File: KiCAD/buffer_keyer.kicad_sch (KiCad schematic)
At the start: 56 parts, among them J1 Conn_01x02_Pin, J2 Conn_01x02_Pin, J3 Conn_01x02_Pin, T1 2N3906, T2 2N3906, U3 MC1496, U4 MCP4921, U6 LM7171xIN, U7 LM7171xIN, U8 MCP4728

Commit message: kicad(bias): build complete grid-bias sheet (Design A: dual OPA454)
New sheet untitled.kicad_sch (sheet name "Bias", file to be renamed
bias.kicad_sch) implementing the OPA454 high-voltage design per the
Grid_Bias_Schematic.pdf design doc:

- LM7805 (U9) generates the +5 V supply rail from +12 V (~30 mA load,
  no heatsink needed at ~270 mW dissipation)
- LM4040DIZ-5.0 (U11) generates a SEPARATE +5 V_REF precision reference
  biased from +12 V via R_Z = 2.2 kΩ; cathode bypassed by C23 (100 nF).
  Drives only R_GA / R_GB (the two OPA454 summing-junction inputs) and
  the cathode-monitor's 1.5 V threshold divider on its own sheet
- Two OPA454 channels (U5 = Tube A, U10 = Tube B) each with R_F = 170 k,
  R_G = 10 k, R_GL = 22 k, R_pad = 1 k, plus 2N7000 bias-slam (Q2, Q3)
  sharing one R_GATE = 10 k. Transfer function V_out = 18·V_DAC - 85
- Shared bypass caps across U5/U10 V+ and V- rails (1 µF X7R bulk +
  100 nF HF on each rail); justified by grid-bias bandwidth being
  effectively DC vs textbook µV-class instrumentation recommendation

Supporting changes:

- New xmitter:OPA454 multi-unit symbol (Unit A = 3-pin op-amp triangle
  with IN-, IN+, OUT; Unit B = 5-pin power/enable block with V+, V-,
  ED, EDCOMM, STATFLG). Built via tools/add_opa454_symbol.py
- xmitter_prj/grid_bias.sch: V2 = 90 V (was 85), V3 = 5 V (was 12) to
  match the PDF design's +5 V / -90 V supply rails; LM4040 stays at 5 V
- pa_cathode_monitor.md: switch comparator V_REF from the bogus
  LM4040DIZ-1.2 (doesn't exist - LM4040 minimum is 2.048 V) to a shared
  LM4040DIZ-5.0 with a 4.7 k / 1 k trim / 1.5 k divider giving 1.5 V
  nominal (1.21 V to 1.74 V across full pot)
- Documentation/grid_bias.md: full subsystem design doc covering
  architecture decisions, transfer function, per-channel topology, BOM,
  inter-sheet I/O, calibration procedure, and open items
- Documentation/kicad_custom_symbols.md: OPA454 entry plus a note on
  the KiCad sub-symbol naming gotcha (NAME_{unit}_{body_style}, not th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
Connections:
- net +3.3V renamed 3V3

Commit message: kicad: assign 1/4 W metal-film through-hole footprint to all resistors
Footprint: Resistor_THT:R_Axial_DIN0207_L6.3mm_D2.5mm_P10.16mm_Horizontal

DIN 0207 is the standard 1/4 W metal-film body size (Vishay MRS25, Yageo
MFR-25, etc., 6.3 mm x 2.5 mm). The relaxed P10.16mm pitch (vs the snug
P7.62mm) gives extra lead-bend room for hand soldering.

- bias.kicad_sch: 10 resistors (R_FA, R_FB, R_GA, R_GB, R_GATE, R_GLA,
  R_GLB, R_PADA, R_PADB, R_Z)
- buffer_keyer.kicad_sch: 25 resistors (R1-R16, RF_OP, RF_OP1, RG_OP,
  RG_OP1, RLA, RLB, R_INJ1, R_INJ2, Re)

All values fit comfortably in the DIN 0207 body, including the three
51-ohm MC1496 emitter resistors (1 % metal film for carrier-null
precision) and the 330 k MCP4728 null-injection isolators.

Co-Authored-By: Claude Opus 4.7 <noreply@anthropic.com>
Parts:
- R1, R10, R11, R12, R13, R14, R15, R16, R2, R3, R4, R5, R6, R7, R8, R9, RF_OP, RF_OP1, RG_OP, RG_OP1, RLA, RLB, R_INJ1, R_INJ2, Re: footprint (none) -> Resistor_THT:R_Axial_DIN0207_L6.3mm_D2.5mm_P10.16mm_Horizontal
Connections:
- net GRID_CTL_B_OUT: now reaches U8.10 (VD)
- net GRID_CTL_A_OUT: now reaches U8.9 (VC)
- no-connect marks 7 -> 5
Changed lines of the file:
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@@
 	)
 	(no_connect
-		(at 68.58 142.24)
-	)
-	(no_connect
 		(at 196.85 63.5)
 	)
@@
 		(at 179.07 71.12)
 	)
-	(no_connect
-		(at 68.58 139.7)
-	)
 	(wire
 		(pts
@@
 		)
 	)
+	(hierarchical_label "GRID_CTL_A_OUT"
+		(shape output)
+		(at 68.58 139.7 0)
+		(effects
+			(font
+				(size 1.27 1.27)
+			)
+			(justify left)
+		)
+	)
 	(hierarchical_label "3V3"
 		(shape input)
@@
 		)
 	)
+	(hierarchical_label "GRID_CTL_B_OUT"
+		(shape output)
+		(at 68.58 142.24 0)
+		(effects
+			(font
+				(size 1.27 1.27)
+			)
+			(justify left)
+		)
+	)
 	(hierarchical_label "SCL"
 		(shape input)
@@
 			)
 		)
-		(property "Footprint" ""
+		(property "Footprint" "Resistor_THT:R_Axial_DIN0207_L6.3mm_D2.5mm_P10.16mm_Horizontal"
 			(at 176.784 94.996 90)
 			(hide yes)
@@
 			)
 		)
-		(property "Footprint" ""
+		(property "Footprint" "Resistor_THT:R_Axial_DIN0207_L6.3mm_D2.5mm_P10.16mm_Horizontal"
 			(at 128.524 70.104 90)
 			(hide yes)
@@
 			)
 		)
-		(property "Footprint" ""
+		(property "Footprint" "Resistor_THT:R_Axial_DIN0207_L6.3mm_D2.5mm_P10.16mm_Horizontal"
 			(at 237.236 77.724 90)
 			(hide yes)
@@
 			)
 		)
-		(property "Footprint" ""
+		(property "Footprint" "Resistor_THT:R_Axial_DIN0207_L6.3mm_D2.5mm_P10.16mm_Horizontal"
 			(at 238.506 48.514 90)
 			(hide yes)
@@
 			)
 		)
-		(property "Footprint" ""
+		(property "Footprint" "Resistor_THT:R_Axial_DIN0207_L6.3mm_D2.5mm_P10.16mm_Horizontal"
 			(at 169.926 82.804 90)
 			(hide yes)
@@
 			)
 		)
-		(property "Footprint" ""
+		(property "Footprint" "Resistor_THT:R_Axial_DIN0207_L6.3mm_D2.5mm_P10.16mm_Horizontal"
 			(at 69.596 104.394 90)
 			(hide yes)
@@
 			)
 		)
-		(property "Footprint" ""
+		(property "Footprint" "Resistor_THT:R_Axial_DIN0207_L6.3mm_D2.5mm_P10.16mm_Horizontal"
 			(at 249.174 43.434 90)
 			(hide yes)
@@
 			)
 		)
-		(property "Footprint" ""
+		(property "Footprint" "Resistor_THT:R_Axial_DIN0207_L6.3mm_D2.5mm_P10.16mm_Horizontal"
 			(at 207.264 69.596 90)
 			(hide yes)
@@
 			)
 		)
-		(property "Footprint" ""
+		(property "Footprint" "Resistor_THT:R_Axial_DIN0207_L6.3mm_D2.5mm_P10.16mm_Horizontal"
 			(at 213.106 44.704 90)
 			(hide yes)
@@
 			)
 		)
-		(property "Footprint" ""
+		(property "Footprint" "Resistor_THT:R_Axial_DIN0207_L6.3mm_D2.5mm_P10.16mm_Horizontal"
 			(at 175.514 57.404 90)
 			(hide yes)
@@
 			)
 		)
-		(property "Footprint" ""
+		(property "Footprint" "Resistor_THT:R_Axial_DIN0207_L6.3mm_D2.5mm_P10.16mm_Horizontal"
 			(at 188.976 94.234 90)
 			(hide yes)
@@
 			)
 		)
-		(property "Footprint" ""
+		(property "Footprint" "Resistor_THT:R_Axial_DIN0207_L6.3mm_D2.5mm_P10.16mm_Horizontal"
 			(at 208.534 104.394 90)
 			(hide yes)
@@
 			)
 		)
-		(property "Footprint" ""
+		(property "Footprint" "Resistor_THT:R_Axial_DIN0207_L6.3mm_D2.5mm_P10.16mm_Horizontal"
 			(at 152.654 54.864 90)
 			(hide yes)
@@
 			)
 		)
-		(property "Footprint" ""
+		(property "Footprint" "Resistor_THT:R_Axial_DIN0207_L6.3mm_D2.5mm_P10.16mm_Horizontal"
 			(at 163.576 59.944 90)
 			(hide yes)
@@
 			)
 		)
-		(property "Footprint" ""
+		(property "Footprint" "Resistor_THT:R_Axial_DIN0207_L6.3mm_D2.5mm_P10.16mm_Horizontal"
 			(at 229.616 33.274 90)
 			(hide yes)
@@
 			)
 		)
-		(property "Footprint" ""
+		(property "Footprint" "Resistor_THT:R_Axial_DIN0207_L6.3mm_D2.5mm_P10.16mm_Horizontal"
 			(at 134.874 39.624 90)
 			(hide yes)
@@
 			)
 		)
-		(property "Footprint" ""
+		(property "Footprint" "Resistor_THT:R_Axial_DIN0207_L6.3mm_D2.5mm_P10.16mm_Horizontal"
 			(at 150.876 91.694 90)
 			(hide yes)
@@
 			)
 		)
-		(property "Footprint" ""
+		(property "Footprint" "Resistor_THT:R_Axial_DIN0207_L6.3mm_D2.5mm_P10.16mm_Horizontal"
 			(at 105.664 114.554 90)
 			(hide yes)
@@
 			)
 		)
-		(property "Footprint" ""
+		(property "Footprint" "Resistor_THT:R_Axial_DIN0207_L6.3mm_D2.5mm_P10.16mm_Horizontal"
 			(at 237.236 70.104 90)
 			(hide yes)
@@
 			)
 		)
-		(property "Footprint" ""
+		(property "Footprint" "Resistor_THT:R_Axial_DIN0207_L6.3mm_D2.5mm_P10.16mm_Horizontal"
 			(at 145.796 47.244 90)
 			(hide yes)
@@
 			)
 		)
-		(property "Footprint" ""
+		(property "Footprint" "Resistor_THT:R_Axial_DIN0207_L6.3mm_D2.5mm_P10.16mm_Horizontal"
 			(at 105.664 96.774 90)
 			(hide yes)
@@
 			)
 		)
-		(property "Footprint" ""
+		(property "Footprint" "Resistor_THT:R_Axial_DIN0207_L6.3mm_D2.5mm_P10.16mm_Horizontal"
 			(at 93.726 104.394 90)
 			(hide yes)
@@
 			)
 		)
-		(property "Footprint" ""
+		(property "Footprint" "Resistor_THT:R_Axial_DIN0207_L6.3mm_D2.5mm_P10.16mm_Horizontal"
 			(at 56.134 96.774 90)
 			(hide yes)
@@
 			)
 		)
-		(property "Footprint" ""
+		(property "Footprint" "Resistor_THT:R_Axial_DIN0207_L6.3mm_D2.5mm_P10.16mm_Horizontal"
 			(at 197.866 109.474 90)
 			(hide yes)
@@
 			)
 		)
-		(property "Footprint" ""
+		(property "Footprint" "Resistor_THT:R_Axial_DIN0207_L6.3mm_D2.5mm_P10.16mm_Horizontal"
 			(at 56.134 114.554 90)
 			(hide yes)

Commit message: kicad+pdf+tools: diode-OR build-out, cap footprints, regen monitor PDF
KiCad bias sheet: complete the cathode-monitor diode-OR combiner
  - D5, D6 = 1N4148 (diode-OR anodes at each LM393 OC output)
  - R24 = 100 kOhm (R_PD pulldown at common GRID_BLOCK_CRASH node)
  - R25 = 4.7 kOhm (second R_PULL so each LM393 OC has its own
    pull-up to +3.3 V, satisfying the diode-OR topology)
  - Closes the "remaining bias-sheet work" item from the cathode-
    monitor spec's open list.

KiCad arduino sheet: add I_CATHODE_A and I_CATHODE_B hierarchical
inputs so the ADC1 path from the bias sheet has a landing point on
the Metro side.

Tools: add assign_cap_footprints.py, a re-runnable script that walks
.kicad_sch files and assigns THT capacitor footprints by value, based
on the parts on the 2026-06-19 Mouser order:
  100nF / 0.1uF  KEMET C410   C_Disc_D5.0mm_W2.5mm_P5.00mm
  10uF           Panasonic    CP_Radial_D5.0mm_P2.00mm
  680nF / 0.68uF WIMA MKP4    C_Rect_L13.0mm_W6.0mm_P10.00mm_FKS3_FKP3_MKS4
  10nF / 0.01uF  Vishay Y5P   C_Disc_D6.0mm_W2.5mm_P5.00mm
  220pF          Knowles mica C_Rect_L7.0mm_W4.5mm_P5.00mm
Only fills empty Footprint fields; never overwrites. Preserves LF
line endings and writes UTF-8 without BOM (KiCad 10 treats a BOM-
prefixed .kicad_sch as empty).

Run output: 10 caps updated on bias sheet, 17 on buffer_keyer sheet.
Values still needing the user to measure (not in this order):
  bias: C17/C18 1uF, C21 0.22uF, C28/C29 1nF
  buffer_keyer: C1 330pF, C13/C14/C15 1uF
  vfo: CF3/CF5 390pF

Cathode_Monitor_Schematic.pdf regenerated with the diode-OR topology
locked in:
  - Schematic page adds L5b diode-OR sub-diagram (D_OR_A horizontal,
    D_OR_B from "Ch. B" annotation, R_PD pulldown, GRID_BLOCK_CRASH
    output)
  - R_SOURCE now drawn explicitly between OPA1641 OUT and LM393 (+)
  - V_REF block replaced with V_THR (R17/RV1/R18 trim, 1.06-2.13 V)
  - BOM, layers table, operating-points action column updated
  - "Watchdog gate" section rewritten: bias s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
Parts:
- C10, C12, C16, C2, C5, C6, C8, C_IN, C_IN1, C_OP_OUT, C_OP_OUT1, Cx1: footprint (none) -> Capacitor_THT:C_Disc_D5.0mm_W2.5mm_P5.00mm
- C11, C4, C7, C9: footprint (none) -> Capacitor_THT:CP_Radial_D5.0mm_P2.00mm
- C3: footprint (none) -> Capacitor_THT:C_Rect_L13.0mm_W6.0mm_P10.00mm_FKS3_FKP3_MKS4
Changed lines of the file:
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@@
 			)
 		)
-		(property "Footprint" ""
+		(property "Footprint" "Capacitor_THT:C_Disc_D5.0mm_W2.5mm_P5.00mm"
 			(at 244.8052 81.28 0)
 			(hide yes)
@@
 			)
 		)
-		(property "Footprint" ""
+		(property "Footprint" "Capacitor_THT:CP_Radial_D5.0mm_P2.00mm"
 			(at 232.1052 143.51 0)
 			(hide yes)
@@
 			)
 		)
-		(property "Footprint" ""
+		(property "Footprint" "Capacitor_THT:C_Disc_D5.0mm_W2.5mm_P5.00mm"
 			(at 27.6352 139.7 0)
 			(hide yes)
@@
 			)
 		)
-		(property "Footprint" ""
+		(property "Footprint" "Capacitor_THT:C_Disc_D5.0mm_W2.5mm_P5.00mm"
 			(at 223.52 91.7448 0)
 			(hide yes)
@@
 			)
 		)
-		(property "Footprint" ""
+		(property "Footprint" "Capacitor_THT:C_Disc_D5.0mm_W2.5mm_P5.00mm"
 			(at 244.8052 121.92 0)
 			(hide yes)
@@
 			)
 		)
-		(property "Footprint" ""
+		(property "Footprint" "Capacitor_THT:C_Disc_D5.0mm_W2.5mm_P5.00mm"
 			(at 228.6 28.2448 0)
 			(hide yes)
@@
 			)
 		)
-		(property "Footprint" ""
+		(property "Footprint" "Capacitor_THT:C_Disc_D5.0mm_W2.5mm_P5.00mm"
 			(at 192.7352 43.18 0)
 			(hide yes)
@@
 			)
 		)
-		(property "Footprint" ""
+		(property "Footprint" "Capacitor_THT:C_Disc_D5.0mm_W2.5mm_P5.00mm"
 			(at 244.8052 143.51 0)
 			(hide yes)
@@
 			)
 		)
-		(property "Footprint" ""
+		(property "Footprint" "Capacitor_THT:C_Disc_D5.0mm_W2.5mm_P5.00mm"
 			(at 90.4748 100.33 0)
 			(hide yes)
@@
 			)
 		)
-		(property "Footprint" ""
+		(property "Footprint" "Capacitor_THT:CP_Radial_D5.0mm_P2.00mm"
 			(at 232.1052 121.92 0)
 			(hide yes)
@@
 			)
 		)
-		(property "Footprint" ""
+		(property "Footprint" "Capacitor_THT:CP_Radial_D5.0mm_P2.00mm"
 			(at 202.8952 43.18 0)
 			(hide yes)
@@
 			)
 		)
-		(property "Footprint" ""
+		(property "Footprint" "Capacitor_THT:CP_Radial_D5.0mm_P2.00mm"
 			(at 82.8548 100.33 0)
 			(hide yes)
@@
 			)
 		)
-		(property "Footprint" ""
+		(property "Footprint" "Capacitor_THT:C_Disc_D5.0mm_W2.5mm_P5.00mm"
 			(at 124.46 53.6448 0)
 			(hide yes)
@@
 			)
 		)
-		(property "Footprint" ""
+		(property "Footprint" "Capacitor_THT:C_Disc_D5.0mm_W2.5mm_P5.00mm"
 			(at 204.47 54.9148 0)
 			(hide yes)
@@
 			)
 		)
-		(property "Footprint" ""
+		(property "Footprint" "Capacitor_THT:C_Disc_D5.0mm_W2.5mm_P5.00mm"
 			(at 187.96 89.2048 0)
 			(hide yes)
@@
 			)
 		)
-		(property "Footprint" ""
+		(property "Footprint" "Capacitor_THT:C_Disc_D5.0mm_W2.5mm_P5.00mm"
 			(at 264.16 30.7848 0)
 			(hide yes)
@@
 			)
 		)
-		(property "Footprint" ""
+		(property "Footprint" "Capacitor_THT:C_Rect_L13.0mm_W6.0mm_P10.00mm_FKS3_FKP3_MKS4"
 			(at 157.1752 63.5 0)
 			(hide yes)

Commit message: tools+kicad: extend cap-footprint map with user-stock disc values
Added 390 pF, 330 pF, 33 pF to assign_cap_footprints.py with
diameter taken from the user's measurement (1/4" body for 390/330 pF,
3/16" for 33 pF) on P5.08 mm pitch.

Re-ran the script:
  buffer_keyer.kicad_sch: C1=330pF -> C_Disc_D6.0mm_W2.5mm_P5.00mm
  vfo.kicad_sch CF3/CF5 (390pF) already had footprints assigned
  manually; left alone (script never overwrites).

Still needing footprints (1uF, 0.22uF, 1nF) -- yet to be ordered:
  bias: C17/C18 1uF, C21 0.22uF, C28/C29 1nF
  buffer_keyer: C13/C14/C15 1uF

Co-Authored-By: Claude Opus 4.7 <noreply@anthropic.com>
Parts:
- C1: footprint (none) -> Capacitor_THT:C_Disc_D6.0mm_W2.5mm_P5.00mm
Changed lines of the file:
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@@
 			)
 		)
-		(property "Footprint" ""
+		(property "Footprint" "Capacitor_THT:C_Disc_D6.0mm_W2.5mm_P5.00mm"
 			(at 222.25 65.0748 0)
 			(hide yes)

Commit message: caps: complete footprint coverage on active sheets + add datasheets
Pending Mouser cart 2026-06-24 (1:31 PM) adds two more KEMET parts
that close the remaining cap gaps:

  KEMET C317C334K3R5TA  0.33 uF X7R  25V  LS=5.08mm  (qty 4)
  KEMET C327C102J3G5TA  1000 pF C0G  25V  LS=5.08mm  (qty 5)

Updated VALUE_TO_FOOTPRINT and re-ran the script:
  bias: C21 0.33uF -> C_Rect_L7.0mm_W3.5mm_P5.00mm
  bias: C28/C29 1nF -> C_Rect_L7.0mm_W3.5mm_P5.00mm

Every capacitor across the active sheets (bias, buffer_keyer, vfo,
arduino) now has a footprint assigned. The 100pF (AVX AR21) mapping
remains for future PA tank / LPF use; no current schematic instance.

Also: Documentation/Components/ added for traceability of part choices:
  90968303_1-3748A_2026-06-19.pdf  -- Mouser invoice (R/Q/LM7171/DAC/etc)
  AR-Series.pdf                    -- AVX SkyCap/AR series MLCC
  C330C105K2R5TA.pdf               -- KEMET 1uF X7R 200V datasheet
  KEM_C1049_GOLDMAX_C0G.pdf        -- KEMET GoldMax C0G series
  KEM_C1050_GOLDMAX_X7R.pdf        -- KEMET GoldMax X7R series

Co-Authored-By: Claude Opus 4.7 <noreply@anthropic.com>
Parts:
- C13, C14, C15: footprint (none) -> Capacitor_THT:C_Rect_L7.2mm_W4.5mm_P5.00mm
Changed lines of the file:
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@@
 			)
 		)
-		(property "Footprint" ""
+		(property "Footprint" "Capacitor_THT:C_Rect_L7.2mm_W4.5mm_P5.00mm"
 			(at 117.8052 50.8 0)
 			(hide yes)
@@
 			)
 		)
-		(property "Footprint" ""
+		(property "Footprint" "Capacitor_THT:C_Rect_L7.2mm_W4.5mm_P5.00mm"
 			(at 35.2552 139.7 0)
 			(hide yes)
@@
 			)
 		)
-		(property "Footprint" ""
+		(property "Footprint" "Capacitor_THT:C_Rect_L7.2mm_W4.5mm_P5.00mm"
 			(at 140.6652 50.8 0)
 			(hide yes)

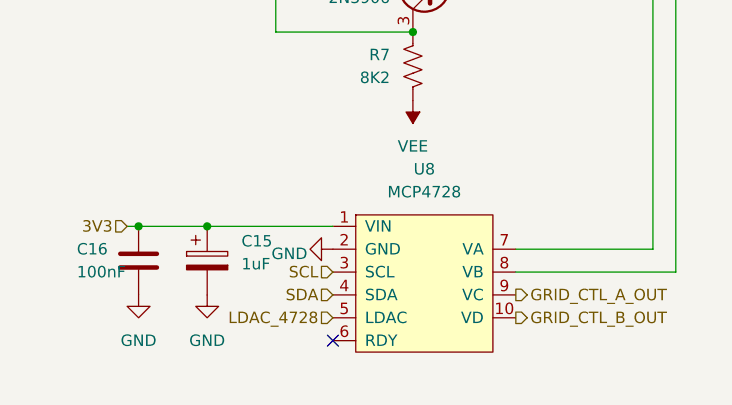
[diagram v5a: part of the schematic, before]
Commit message: front-panel: QT encoder swap, PCF8575 breakout, pre-fab checklist, INT-none decision
Switch STEP + FUNC from direct PCF8575 GPIO to Adafruit I2C QT Rotary
Encoder breakouts (PID 4991) at addr 0x36 / 0x37. The onboard seesaw
SAMD09 handles quadrature decoding + button debounce, dropping ~200
lines of firmware. PCF8575 still covers the LCD (4-bit), paddle, and
panel LEDs.

Add custom KiCad symbols + footprints for both new breakouts to
xmitter.kicad_sym and xmitter.pretty. Footprint properties on the new
symbols are pre-linked, so schematic instances auto-associate. Some
coordinates in both footprints are best-guess pending physical
measurement -- flagged in the descr fields and in the new
front_panel_interface.md open-items subsections.

Decision documented (2026-07-03): no INT wiring back to the Metro.
Firmware polls all three I2C devices at 100 Hz; velocity-adaptive VFO
tuning is computed from delta-position / delta-time in the poll loop.
Rationale and a "here's how to add INT later" path in the new
"Interrupt handling (decision: none)" section of
front_panel_interface.md.

New Documentation/pcb_fab_checklist.md is the consolidated pre-flight
gate before analog-board gerbers ship -- nine sections covering
footprint verification, schematic completeness, ERC/DRC, physical, and
BOM sign-offs. build_checklist.md and CLAUDE.md updated to point at it.

Also in this bundle: SDA/SCL hierarchical labels changed to
bidirectional shape on the VFO, buffer_keyer, and interface sheets
(was an output/input polarity soup that would have failed ERC).
Interface and Front_Panel child sheets registered in .kicad_pro.
Front_Panel is an empty stub; components go in when the sheet is
populated. Adafruit PCF8575 and QT rotary encoder datasheets committed
under Documentation/Components/.

Co-Authored-By: Claude Opus 4.7 <noreply@anthropic.com>
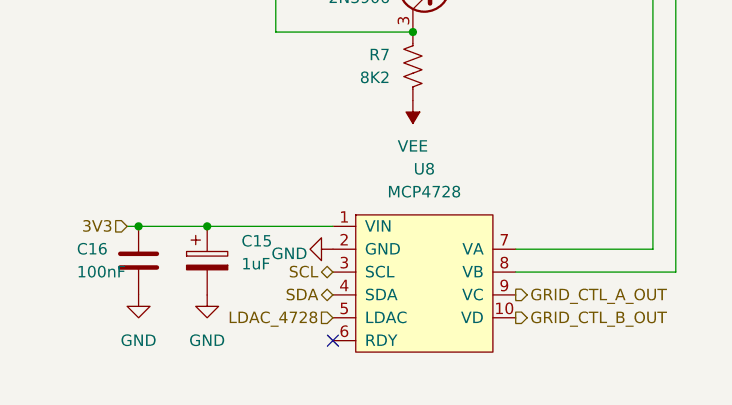
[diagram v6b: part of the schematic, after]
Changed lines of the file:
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@@
 	)
 	(hierarchical_label "SDA"
-		(shape input)
+		(shape bidirectional)
 		(at 48.26 139.7 180)
 		(effects
@@
 	)
 	(hierarchical_label "SCL"
-		(shape input)
+		(shape bidirectional)
 		(at 48.26 137.16 180)
 		(effects
